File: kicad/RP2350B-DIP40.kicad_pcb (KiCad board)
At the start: 2 copper layers, 54 x 21.6 mm, 30 parts, among them J1 USB_C_Receptacle_USB2.0_16P, J2 Conn_ARM_JTAG_SWD_10, J3 Conn_01x03_Socket, J4 qwiic, J5 Micro_SD_Card, U1 TPD2EUSB30, U2 Picossci_B2_RB2350B, U3 18F47Q43, U4 TPS22917DBV

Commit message: Add PCB design RP2350B-DIP40-rev1.0
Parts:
- removed TP1: TestPoint, TestPoint:TestPoint_Pad_1.0x1.0mm
- J2: value Conn_ARM_JTAG_SWD_10 -> debug connector; footprint Connector_PinHeader_1.27mm:PinHeader_2x05_P1.27mm_Vertical_SMD -> Connector_JST:JST_SH_SM03B-SRSS-TB_1x03-1MP_P1.00mm_Horizontal
- J3: value Conn_01x03_Socket -> uart connector
- R4: value 10K -> 33R; moved to F.Cu
- R5: moved to F.Cu
- moved R5 13.8 mm to (153.6, 131.3), turned to 180 degrees
- moved R4 13.3 mm to (153.6, 122.9), turned to 180 degrees
- moved J3 2.71 mm to (156.0, 127.1)
- moved R9 1.98 mm to (140.3, 123.7)
- moved R3 1.73 mm to (112.4, 113.9)
- moved C4 0.79 mm to (128.5, 115.5)
- moved J2 0.71 mm to (156.0, 117.7), turned to 90 degrees
- moved R8 0.39 mm to (130.7, 118.6)
- moved U1 0.13 mm to (113.0, 120.4)
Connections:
- J2 pad 1: +3.3V -> SWCLK
- J2 pad 2: SWDIO -> GND
- J2 pad 3: GND -> SWDIO
- J3 pad 1: GND -> Net-(J3-RX)
- J3 pad 2: UART0_RX -> GND
- J3 pad 3: UART0_TX -> Net-(J3-TX)
- R4 pad 1: +3.3V -> Net-(J3-TX)
- R4 pad 2: nRESET -> UART0_TX
- R5 pad 1: SWCLK -> Net-(J3-RX)
- R5 pad 2: Net-(J2-SWCLK/TCK) -> UART0_RX
- U2 pad 10: SCK -> RB6
- U2 pad 11: MOSI -> RB7
- U2 pad 30: unconnected-(U2-GP24(LED1)-Pad30) -> RD0
- U2 pad 31: unconnected-(U2-GP25(LED2)-Pad31) -> RD1
- U2 pad 32: SWO -> RD2
- U2 pad 33: 5V_OUT_EN -> RD3
- U2 pad 34: RE0 -> RD4
- U2 pad 35: RE1 -> RD5
- U2 pad 36: RE2 -> RD6
- U2 pad 37: RE3 -> RD7
- U2 pad 38: RD0 -> unconnected-(U2-GP32-Pad38)
- U2 pad 39: RD1 -> unconnected-(U2-GP33-Pad39)
- U2 pad 4: UART0_TX -> RB0
- U2 pad 40: RD2 -> unconnected-(U2-GP34-Pad40)
- U2 pad 41: RD3 -> 5V_OUT_EN
- U2 pad 42: RD4 -> RE0
- U2 pad 43: RD5 -> RE1
- U2 pad 44: RD6 -> RE2
- U2 pad 45: RD7 -> RE3
- U2 pad 47: RB0 -> MISO
- U2 pad 48: RB1 -> SPI_CS
- U2 pad 49: RB2 -> SCK
- U2 pad 5: UART0_RX -> RB1
- U2 pad 50: RB3 -> MOSI
- U2 pad 51: RB4 -> UART0_TX
- U2 pad 52: RB5 -> UART0_RX
- U2 pad 53: RB6 -> SDA
- U2 pad 54: RB7 -> SCL
- U2 pad 6: SDA -> RB2
- U2 pad 7: SCL -> RB3
- U2 pad 8: MISO -> RB4
- U2 pad 9: SPI_CS -> RB5
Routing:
- net nRESET: track 68.8 -> 0.00 mm, vias 3 -> 0
- net +3.3V: track 88.7 -> 66.2 mm, vias 6 -> 5
- net Net-(J2-SWCLK/TCK): track 20.9 -> 0.00 mm, vias 3 -> 0
- net RB0: track 3.84 -> 22.3 mm
- net RB7: track 15.4 -> 33.8 mm
- net RB6: track 13.9 -> 31.0 mm
- net RB5: track 12.7 -> 28.1 mm
- net RD0: track 38.3 -> 23.1 mm, vias 1 -> 3
- net RB4: track 11.4 -> 26.0 mm
- net SWO: track 14.4 -> 0.00 mm, vias 2 -> 0
- net RD3: track 28.9 -> 15.7 mm, vias 3 -> 1
- net RB3: track 10.2 -> 23.4 mm
- net RB2: track 7.08 -> 20.2 mm
- net RD2: track 31.1 -> 18.0 mm
- net RE1: track 33.1 -> 21.3 mm, vias 3 -> 1
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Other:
- board text added: "@hanyazou Mar 22, 2026"
- board text added: "CLK"
- board text added: "DIO"
- board text added: "RP2350B-DIP40 rev 1.0"
- board text added: "RX←"
- board text added: "TX→"
- board text removed: "RP2350B-DIP40 rev 0.8 @hanyazou Mar 7, 2026"
- board text removed: "←TX"
- board text removed: "→ RX"

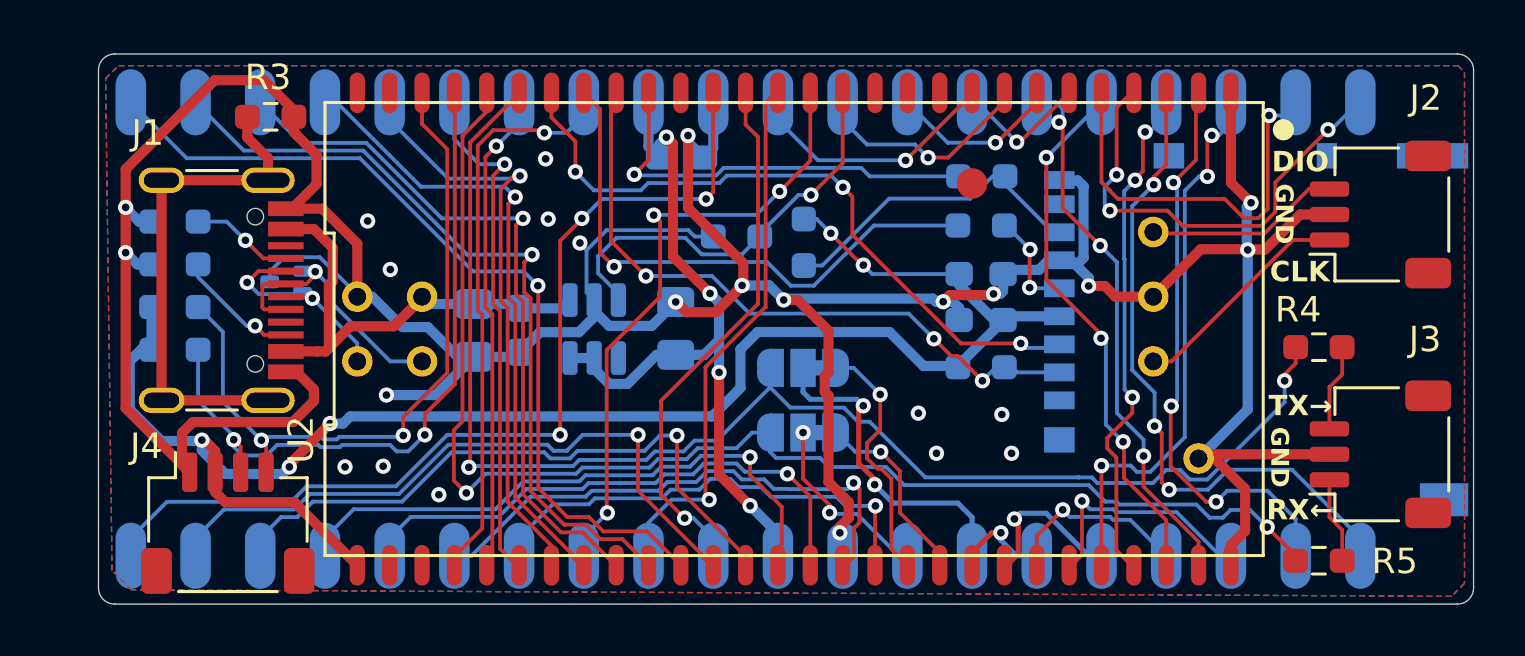
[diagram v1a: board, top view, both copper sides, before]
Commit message: Add PCB design RP2350B-DIP40-rev1.1
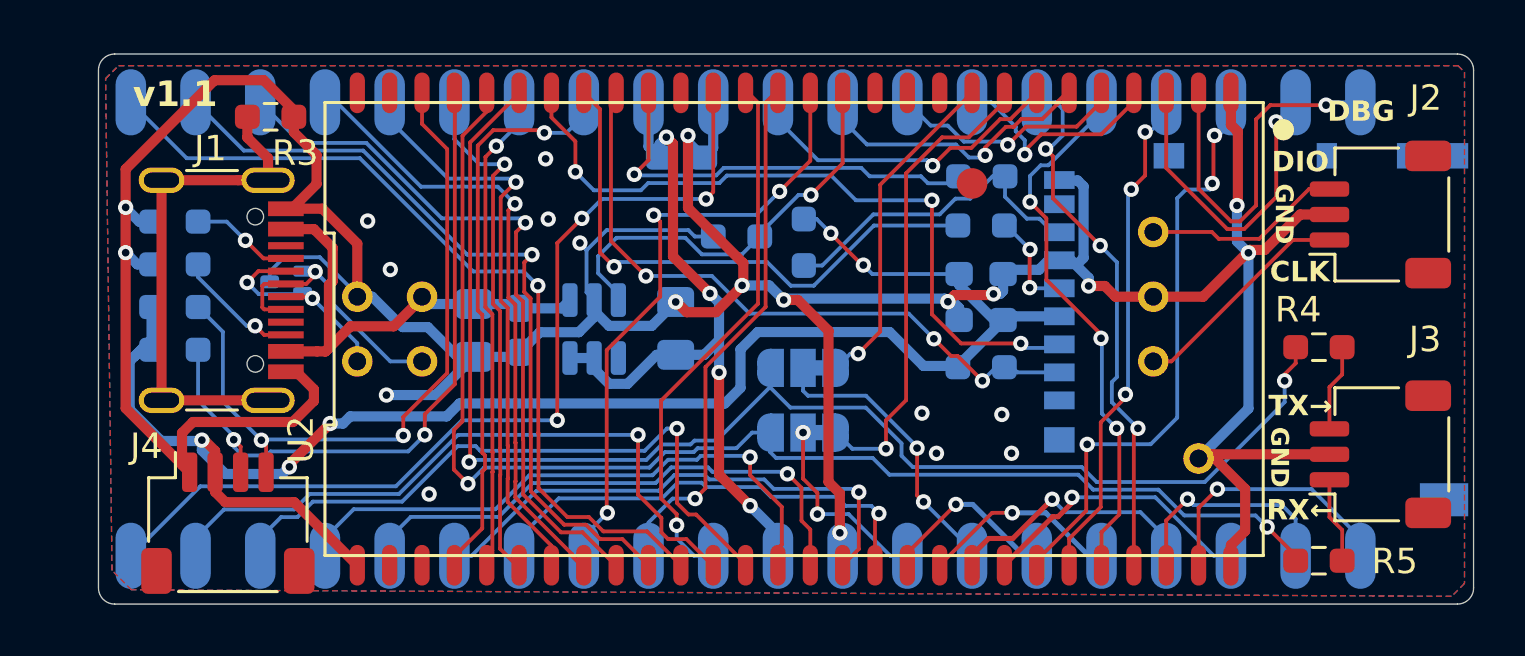
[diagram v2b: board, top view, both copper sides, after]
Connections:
- U2 pad 18: GP14 -> RC0
- U2 pad 19: GP15 -> RC1
- U2 pad 20: RC0 -> RC2
- U2 pad 21: RC1 -> RC3
- U2 pad 22: RC2 -> RC4
- U2 pad 23: RC3 -> RC5
- U2 pad 24: RC4 -> RC6
- U2 pad 25: RC5 -> RC7
- U2 pad 26: RC6 -> RD0
- U2 pad 27: RC7 -> RD1
- U2 pad 30: RD0 -> RD2
- U2 pad 31: RD1 -> RD3
- U2 pad 32: RD2 -> RD4
- U2 pad 33: RD3 -> RD5
- U2 pad 34: RD4 -> RD6
- U2 pad 35: RD5 -> RD7
- U2 pad 36: RD6 -> GP15
- U2 pad 37: RD7 -> GP14
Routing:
- net RD1: track 26.4 -> 10.4 mm, vias 3 -> 1
- net RD0: track 23.1 -> 8.95 mm, vias 3 -> 1
- net GP15: track 7.47 -> 18.7 mm
- net RD4: track 5.26 -> 9.03 mm
- net GP14: track 9.82 -> 13.2 mm
- net RC2: track 7.41 -> 10.8 mm
- net RD2: track 18.0 -> 14.7 mm, vias 3 -> 1
- net RC0: track 3.91 -> 7.19 mm
- net RD3: track 15.7 -> 12.8 mm
- net RD7: track 10.4 -> 13.1 mm
- net RD5: track 6.77 -> 9.36 mm
- net RD6: track 8.91 -> 11.5 mm
- net RC1: track 6.36 -> 8.40 mm
- net MOSI: track 26.8 -> 28.5 mm
- net RC3: track 9.53 -> 11.2 mm
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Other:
- board text added: "1"
- board text added: "10"
- board text added: "13"
- board text added: "14"
- board text added: "15"
- board text added: "16"
- board text added: "17"
- board text added: "18"
- board text added: "19"
- board text added: "2"
- board text added: "20"
- board text added: "21"
- board text added: "22"
- board text added: "23"
- board text added: "24"
- board text added: "25"
- board text added: "26"
- board text added: "27"
- board text added: "28"
- board text added: "29"
- board text added: "3"
- board text added: "30"
- board text added: "33"
- board text added: "34"
- board text added: "35"
- board text added: "36"
- board text added: "37"
- board text added: "38"
- board text added: "39"
- board text added: "4"
- board text added: "40"
- board text added: "5"
- board text added: "5V"
- board text added: "6"
- board text added: "7"
- board text added: "8"
- board text added: "9"
- board text added: "@hanyazou Apr 18, 2026"
- board text added: "DBG"
- board text added: "RP2350B-DIP40 rev 1.1"
- board text added: "v1.1"
- board text removed: "@hanyazou Mar 22, 2026"
- board text removed: "RP2350B-DIP40 rev 1.0"
